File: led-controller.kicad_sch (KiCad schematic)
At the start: 1 part, among them U1 ESP32-DevKitC

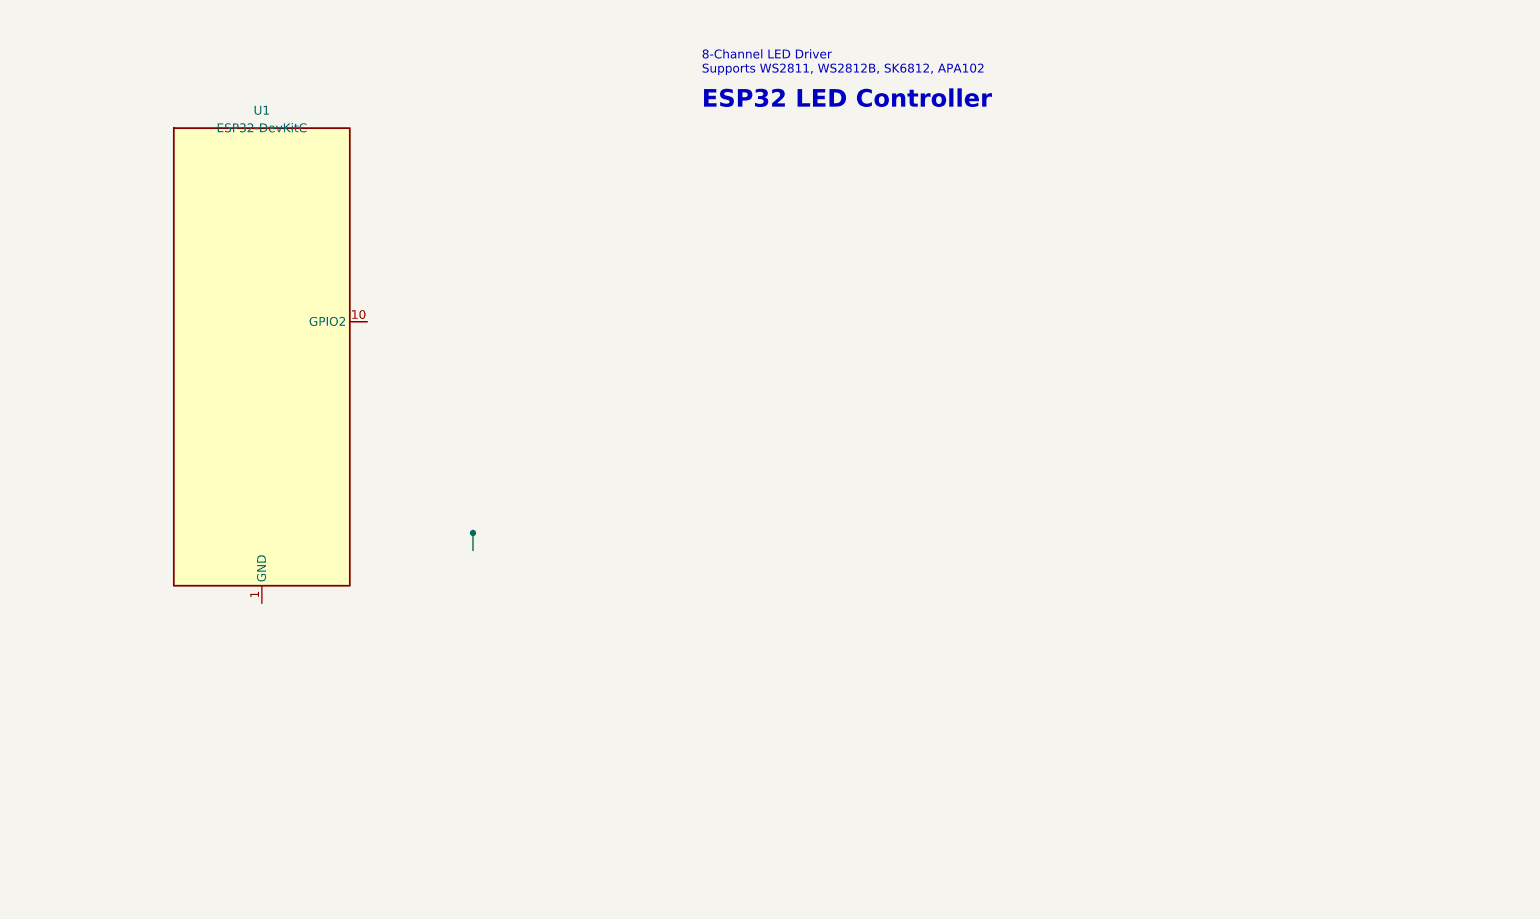
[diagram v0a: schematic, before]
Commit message: Fix missing electronic components
Update KiCad project to include all components.
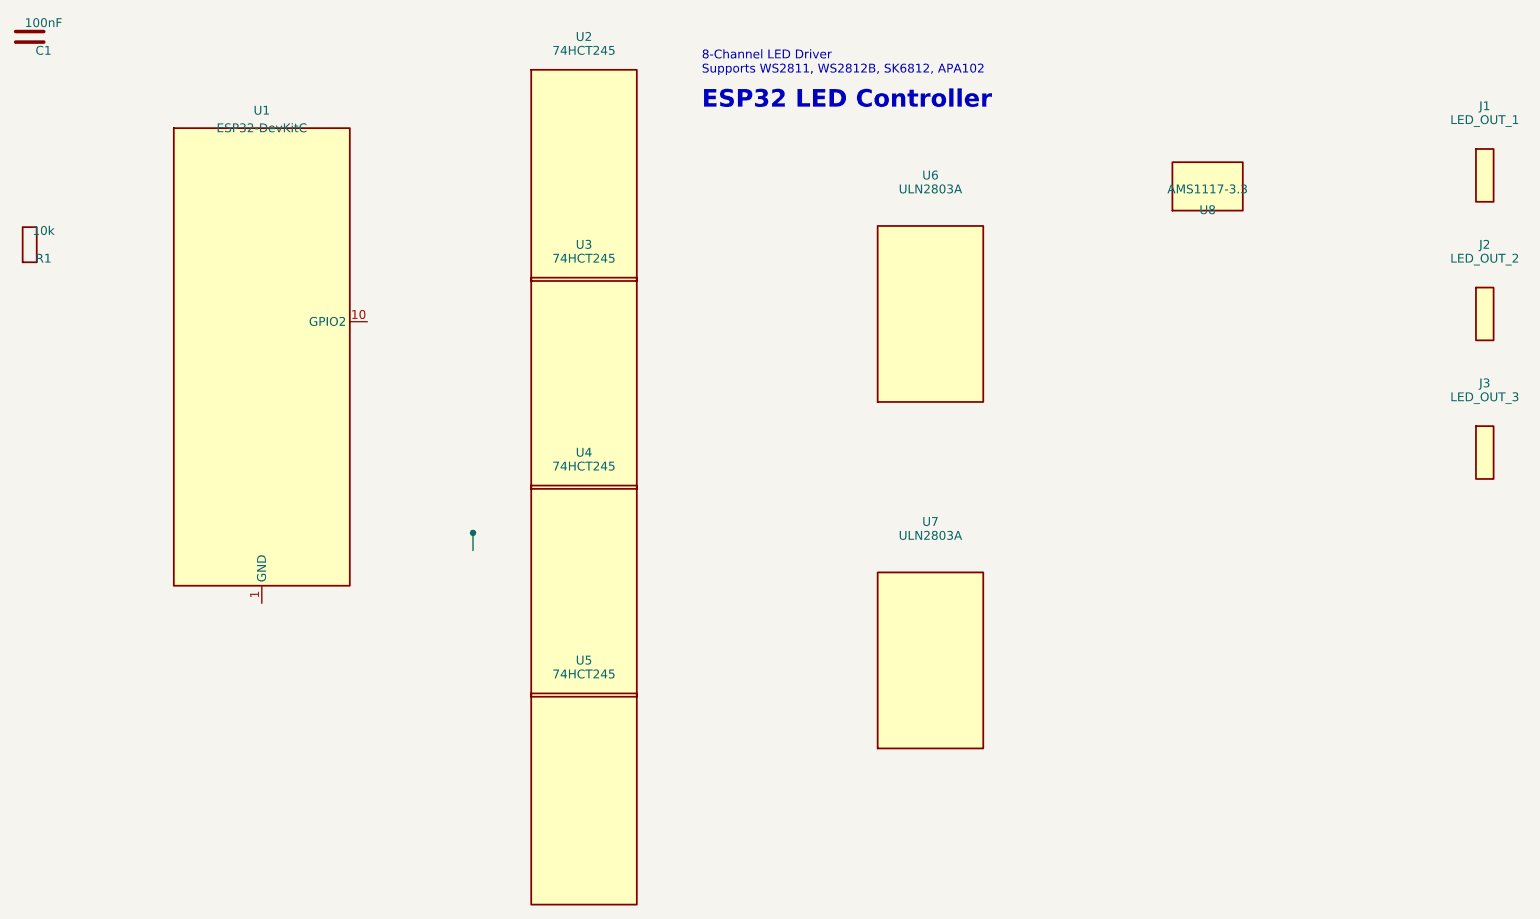
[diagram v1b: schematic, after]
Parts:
- added C1: 100nF, Capacitor_SMD:C_0805_2012Metric, symbol Device:C
- added J1: LED_OUT_1, TerminalBlock:TerminalBlock_bornier-3_P5.08mm, symbol Connector:Screw_Terminal_01x03
- added J2: LED_OUT_2, TerminalBlock:TerminalBlock_bornier-3_P5.08mm, symbol Connector:Screw_Terminal_01x03
- added J3: LED_OUT_3, TerminalBlock:TerminalBlock_bornier-3_P5.08mm, symbol Connector:Screw_Terminal_01x03
- added R1: 10k, Resistor_SMD:R_0805_2012Metric, symbol Device:R
- added U2, U3, U4, U5: 74HCT245, Package_DIP:DIP-20_W7.62mm, symbol Logic_74xx:74HCT245
- added U6, U7: ULN2803A, Package_DIP:DIP-18_W7.62mm, symbol Driver_LED:ULN2803A
- added U8: AMS1117-3.3, Package_TO_SOT_SMD:SOT-223-3_TabPin2, symbol Regulator_Linear:AMS1117-3.3
